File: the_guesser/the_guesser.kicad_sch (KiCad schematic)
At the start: 17 parts, among them Q1 2N7002, U1 ESP32-S3, U10 TPS61033DRLR, U11 W25Q128JVS, X2 ECS-3953M-400-AU-TR

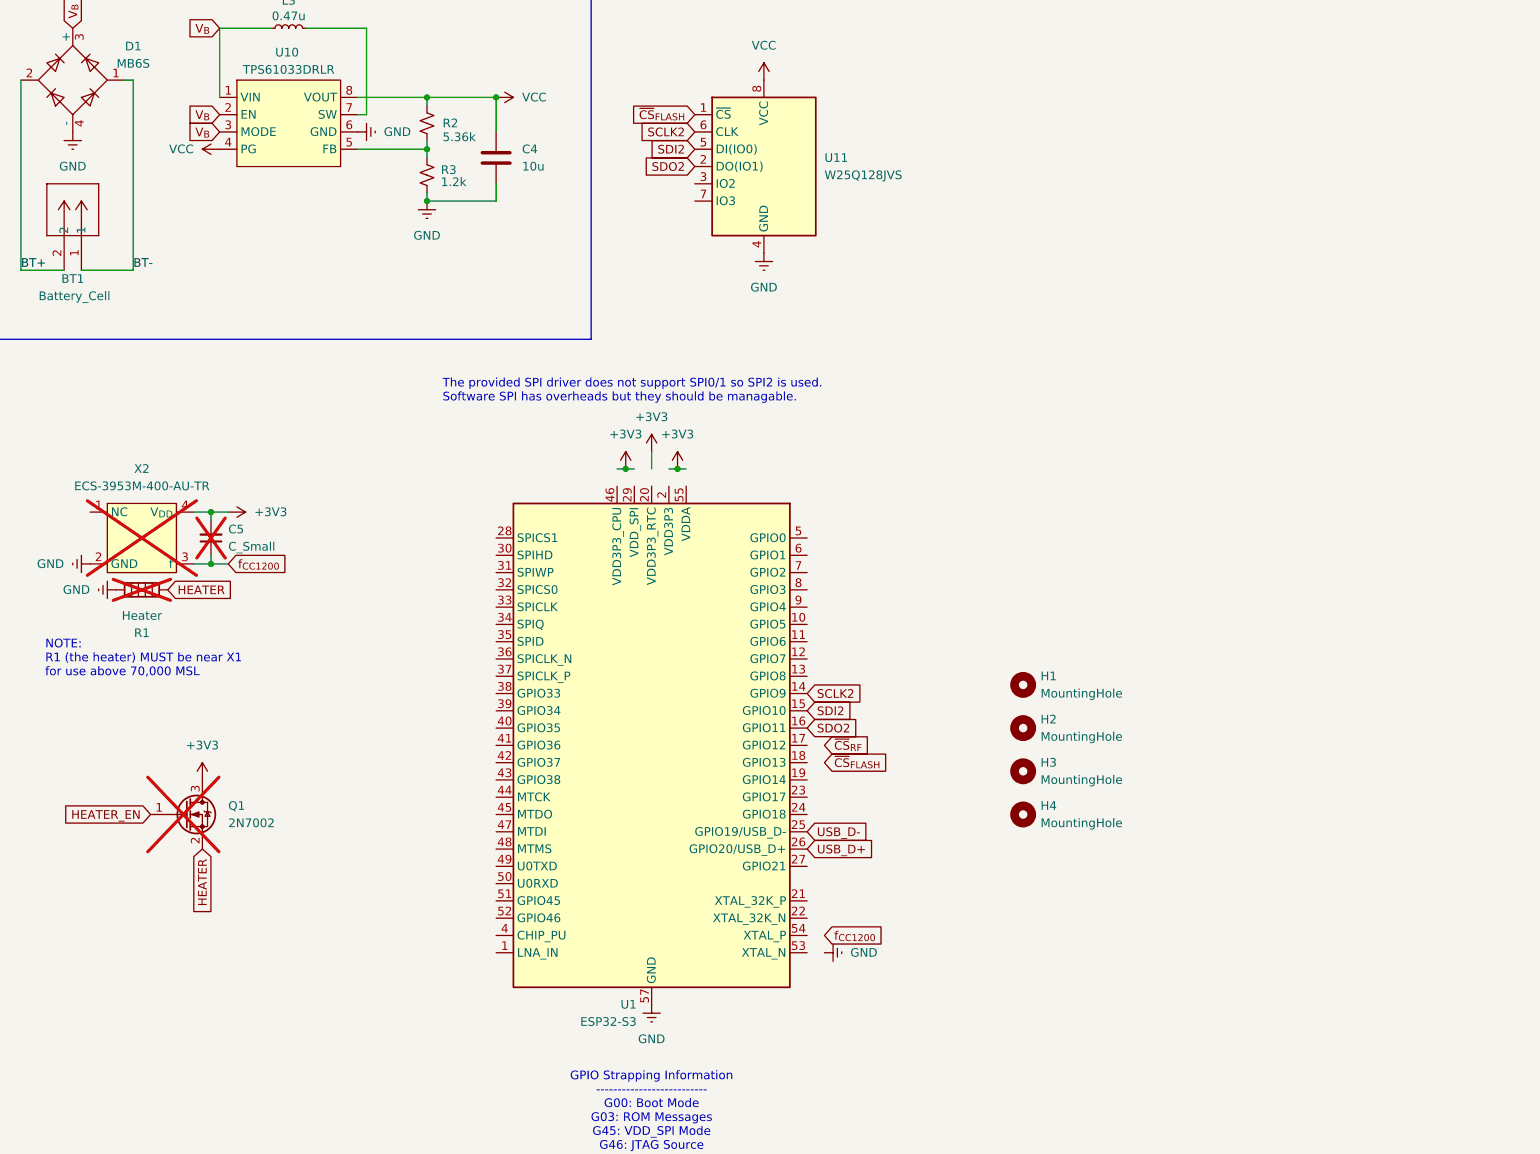
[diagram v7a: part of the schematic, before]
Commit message: Finished Guesser sensor selection and started sensor routing
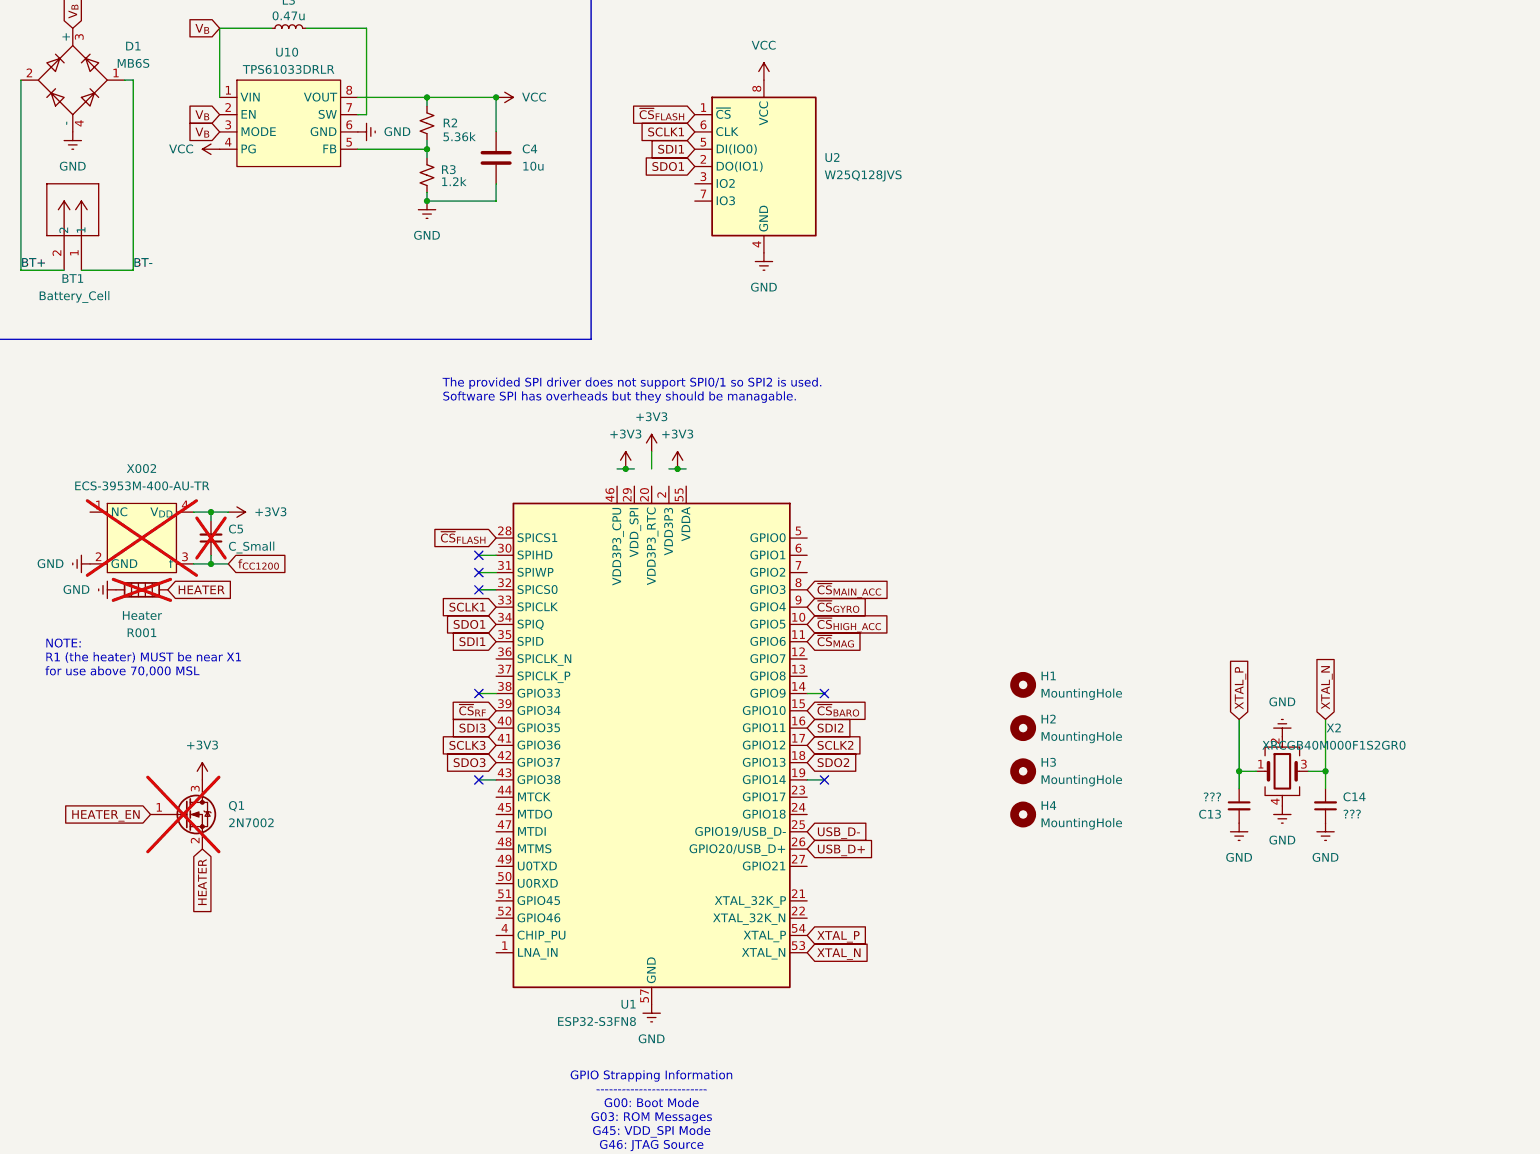
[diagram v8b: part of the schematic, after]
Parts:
- added C13, C14: ???, Capacitor_SMD:C_0603_1608Metric, symbol Device:C_Small
- added X2: XRCGB40M000F1S2GR0, Crystal:Crystal_SMD_2016-4Pin_2.0x1.6mm, symbol Device:Crystal_GND24
- U1: value ESP32-S3 -> ESP32-S3FN8; DKPN (none) -> 1965-ESP32-S3FN8-ND
- renumbered R1 to R001, U11 to U2, X2 to X002
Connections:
- net GND: now also C13.2, C14.1, X2.2, X2.4
- net SCLK2: now also U1.17 (GPIO12); no longer U1.14 (GPIO9), U2.6 (CLK)
- net SDI2: now also U1.16 (GPIO11); no longer U1.15 (GPIO10), U2.5 (DI(IO0))
- net SDO2: now also U1.18 (GPIO13); no longer U1.16 (GPIO11), U2.2 (DO(IO1))
- net ~{CS}_{FLASH}: now also U1.28 (SPICS1)
- net ~{CS}_{RF}: now also U1.39 (GPIO34)
- net ~{CS}_{HIGH_ACC}: now reaches U1.10 (GPIO5)
- net ~{CS}_{MAG}: now reaches U1.11 (GPIO6)
- net SCLK1: now reaches U1.33 (SPICLK)
- net SCLK1: now also U2.6 (CLK)
- net SDO1: now reaches U1.34 (SPIQ)
- net SDO1: now also U2.2 (DO(IO1))
- net SDI1: now reaches U1.35 (SPID)
- net SDI1: now also U2.5 (DI(IO0))
- net SDI3: now reaches U1.40 (GPIO35)
- net SCLK3: now reaches U1.41 (GPIO36)
- net SDO3: now reaches U1.42 (GPIO37)
- net XTAL_N: now reaches U1.53 (XTAL_N)
- net XTAL_N: now also C14.2, X2.3
- net XTAL_P: now reaches U1.54 (XTAL_P)
- net XTAL_P: now also C13.1, X2.1
- net ~{CS}_{MAIN_ACC}: now reaches U1.8 (GPIO3)
- net ~{CS}_{GYRO}: now reaches U1.9 (GPIO4)
- new net ~{CS}_{BARO}: U1.15 (GPIO10)
- no-connect marks 0 -> 7
